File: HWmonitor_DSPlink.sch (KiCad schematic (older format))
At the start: 99 parts, among them J1 Mini USB - Type B, J2 IDC-Header 2x4, T1 760390014, U1 FT232RL, U10 OPA197xDBV, U11 OPA197xDBV, U12 USBLC6-2SC6, U2 ISO7830DWW, U3 ISO7821DWW, U4 SN6501DBVR, U5 TL431BCDBZ, U6 AD5324ARMZ, U7 TLV70450DBVT, U8 OPA197xDBV, U9 OPA197xDBV, X1 Conn_Coaxial, X2 Conn_Coaxial, X3 Conn_Coaxial, X4 Conn_Coaxial

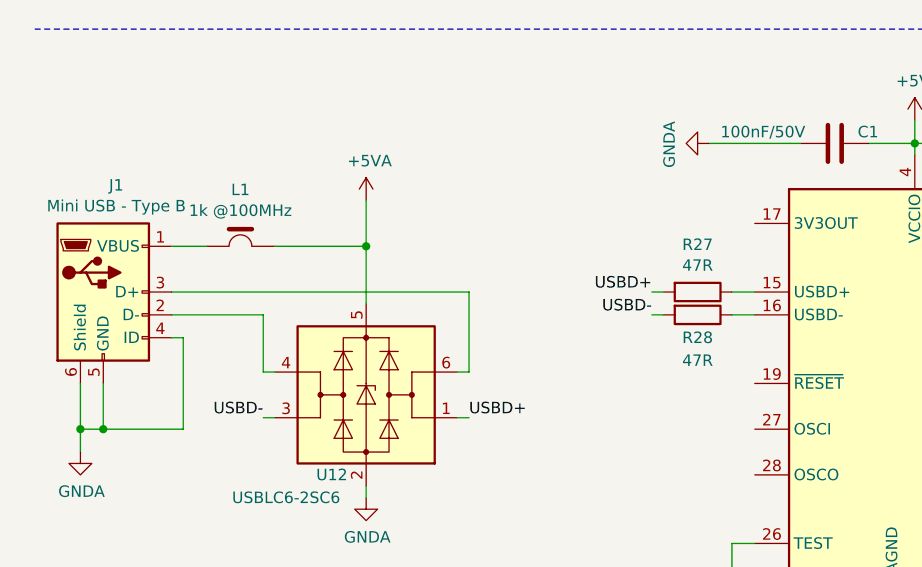
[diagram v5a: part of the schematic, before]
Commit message: modified layout ftdi chip, added 3.3V capacitor
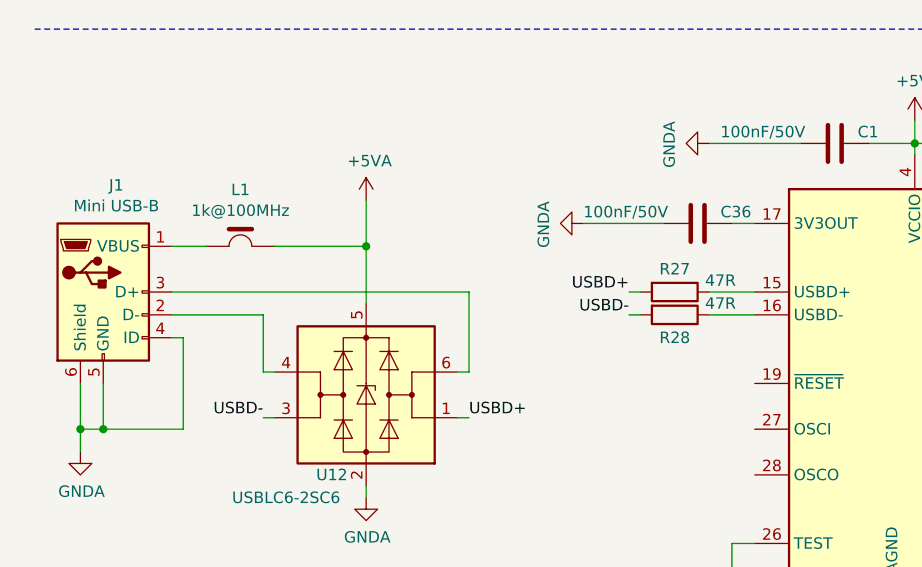
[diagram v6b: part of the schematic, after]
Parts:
- added C36: 100nF/50V, Capacitor_SMD:C_0603_1608Metric, symbol Device:C
- J1: value Mini USB - Type B -> Mini USB-B
- L1: value 1k @100MHz -> 1k@100MHz
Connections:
- net GNDA: now also C36.1
- net at U1.17 (3V3OUT): now also C36.2
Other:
- moved on the sheet: R27, R28
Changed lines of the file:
@@
 AR Path="/60E0A151/610C42BB" Ref="J?"  Part="1"
 F 0 "J1" H 1307 9517 50  0000 C CNN
-F 1 "Mini USB - Type B" H 1307 9426 50  0000 C CNN
+F 1 "Mini USB-B" H 1307 9426 50  0000 C CNN
 F 2 "Connector_USB:USB_Mini-B_Lumberg_2486_01_Horizontal" H 1400 9000 50  0001 C CNN
 F 3 "~" H 1400 9000 50  0001 C CNN
@@
 P 1850 8850
 F 0 "L1" H 1850 9097 50  0000 C CNN
-F 1 "1k @100MHz" H 1850 9006 50  0000 C CNN
+F 1 "1k@100MHz" H 1850 9006 50  0000 C CNN
 F 2 "Inductor_SMD:L_0603_1608Metric" H 1850 8850 50  0001 C CNN
 F 3 "" H 1850 8850 50  0001 C CNN
@@
 $EndComp
 $Comp
-L Device:R R27
-U 1 1 5FEE3BD6
-P 3850 9050
-F 0 "R27" V 3643 9050 50  0000 C CNN
-F 1 "47R" V 3734 9050 50  0000 C CNN
-F 2 "Resistor_SMD:R_0603_1608Metric" V 3780 9050 50  0001 C CNN
-F 3 "~" H 3850 9050 50  0001 C CNN
-	1    3850 9050
-	0    1    1    0
-$EndComp
-$Comp
 L Device:R R28
 U 1 1 5FEE4D7D
-P 3850 9150
-F 0 "R28" V 3950 9150 50  0000 C CNN
-F 1 "47R" V 4050 9150 50  0000 C CNN
-F 2 "Resistor_SMD:R_0603_1608Metric" V 3780 9150 50  0001 C CNN
-F 3 "~" H 3850 9150 50  0001 C CNN
-	1    3850 9150
-	0    1    1    0
-$EndComp
-Wire Wire Line
-	4000 9050 4100 9050
-Wire Wire Line
-	4000 9150 4100 9150
+P 3750 9150
+F 0 "R28" V 3850 9150 50  0000 C CNN
+F 1 "47R" V 3700 9350 50  0000 C CNN
+F 2 "Resistor_SMD:R_0603_1608Metric" V 3680 9150 50  0001 C CNN
+F 3 "~" H 3750 9150 50  0001 C CNN
+	1    3750 9150
+	0    1    1    0
+$EndComp
+Wire Wire Line
+	3900 9050 4100 9050
+Wire Wire Line
+	3900 9150 4100 9150
 $Comp
 L Power_Protection:USBLC6-2SC6 U12
@@
 	4300 8400 3900 8400
 Wire Wire Line
-	3700 9050 3650 9050
-Wire Wire Line
-	3700 9150 3650 9150
-Text Label 3650 9050 2    50   ~ 0
+	3600 9050 3550 9050
+Wire Wire Line
+	3600 9150 3550 9150
+Text Label 3550 9050 2    50   ~ 0
 USBD+
-Text Label 3650 9150 2    50   ~ 0
+Text Label 3550 9150 2    50   ~ 0
 USBD-
 Wire Wire Line
@@
 	1    0    0    -1
 $EndComp
+$Comp
+L Device:C C36
+U 1 1 5FE68C23
+P 3850 8750
+F 0 "C36" V 3800 8650 50  0000 R CNN
+F 1 "100nF/50V" V 3800 9250 50  0000 R CNN
+F 2 "Capacitor_SMD:C_0603_1608Metric" H 3888 8600 50  0001 C CNN
+F 3 "~" H 3850 8750 50  0001 C CNN
+	1    3850 8750
+	0    -1   1    0
+$EndComp
+$Comp
+L Device:R R27
+U 1 1 5FEE3BD6
+P 3750 9050
+F 0 "R27" V 3650 9050 50  0000 C CNN
+F 1 "47R" V 3700 9250 50  0000 C CNN
+F 2 "Resistor_SMD:R_0603_1608Metric" V 3680 9050 50  0001 C CNN
+F 3 "~" H 3750 9050 50  0001 C CNN
+	1    3750 9050
+	0    1    1    0
+$EndComp
+Wire Wire Line
+	4000 8750 4100 8750
+$Comp
+L power:GNDA #PWR0101
+U 1 1 5FEF754F
+P 3350 8750
+AR Path="/5FEF754F" Ref="#PWR0101"  Part="1"
+AR Path="/60E0A151/5FEF754F" Ref="#PWR?"  Part="1"
+F 0 "#PWR0101" H 3350 8500 50  0001 C CNN
+F 1 "GNDA" H 3355 8577 50  0000 C CNN
+F 2 "" H 3350 8750 50  0001 C CNN
+F 3 "" H 3350 8750 50  0001 C CNN
+	1    3350 8750
+	0    1    1    0
+$EndComp
+Wire Wire Line
+	3700 8750 3350 8750
 $EndSCHEMATC

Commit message: last modifications, documents generated
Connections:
- net GNDA: no longer J1.4 (ID)
- no-connect marks 0 -> 15
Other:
- note added: "HWmonitor & DSPcom debug tool"
- note removed: "HWmonitor & DSPlink debug tool"
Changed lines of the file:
@@
-$EndComp
-$Comp
-L Connector:USB_B_Mini J1
-U 1 1 610C42BB
-P 1250 9050
-AR Path="/610C42BB" Ref="J1"  Part="1"
-AR Path="/60E0A151/610C42BB" Ref="J?"  Part="1"
-F 0 "J1" H 1307 9517 50  0000 C CNN
-F 1 "Mini USB-B" H 1307 9426 50  0000 C CNN
-F 2 "Connector_USB:USB_Mini-B_Lumberg_2486_01_Horizontal" H 1400 9000 50  0001 C CNN
-F 3 "~" H 1400 9000 50  0001 C CNN
-F 4 "65100516121" H 1250 9050 50  0001 C CNN "MPN"
-	1    1250 9050
-	1    0    0    -1
 $EndComp
 $Comp
@@
 Connection ~ 4700 10500
 Wire Wire Line
-	1550 9250 1600 9250
-Wire Wire Line
-	1600 9250 1600 9650
-Wire Wire Line
-	1600 9650 1250 9650
-Wire Wire Line
 	1250 9650 1250 9450
 Wire Wire Line
@@
 Wire Wire Line
 	1150 9650 1250 9650
-Connection ~ 1250 9650
 $Comp
 L #MyLibrary:Ferrite_Bead L1
@@
 $EndComp
 Text Notes 12350 10350 0    126  Italic 25
-HWmonitor & DSPlink debug tool
+HWmonitor & DSPcom debug tool
 $Comp
 L #MyLibrary:TLV70450DBVT U7
@@
 Wire Wire Line
 	3700 8750 3350 8750
+NoConn ~ 4100 9450
+NoConn ~ 4100 9650
+NoConn ~ 4100 9850
+NoConn ~ 5700 10150
+NoConn ~ 5700 10050
+NoConn ~ 5700 9950
+NoConn ~ 5700 9450
+NoConn ~ 5700 9350
+NoConn ~ 5700 9250
+NoConn ~ 5700 9150
+NoConn ~ 5700 9050
+NoConn ~ 5700 8950
+NoConn ~ 2750 5400
+NoConn ~ 8900 3600
+$Comp
+L Connector:USB_B_Mini J1
+U 1 1 610C42BB
+P 1250 9050
+AR Path="/610C42BB" Ref="J1"  Part="1"
+AR Path="/60E0A151/610C42BB" Ref="J?"  Part="1"
+F 0 "J1" H 1307 9517 50  0000 C CNN
+F 1 "Mini USB-B" H 1307 9426 50  0000 C CNN
+F 2 "Connector_USB:USB_Mini-B_Lumberg_2486_01_Horizontal" H 1400 9000 50  0001 C CNN
+F 3 "~" H 1400 9000 50  0001 C CNN
+F 4 "65100516121" H 1250 9050 50  0001 C CNN "MPN"
+	1    1250 9050
+	1    0    0    -1
+$EndComp
+NoConn ~ 1550 9250
 $EndSCHEMATC

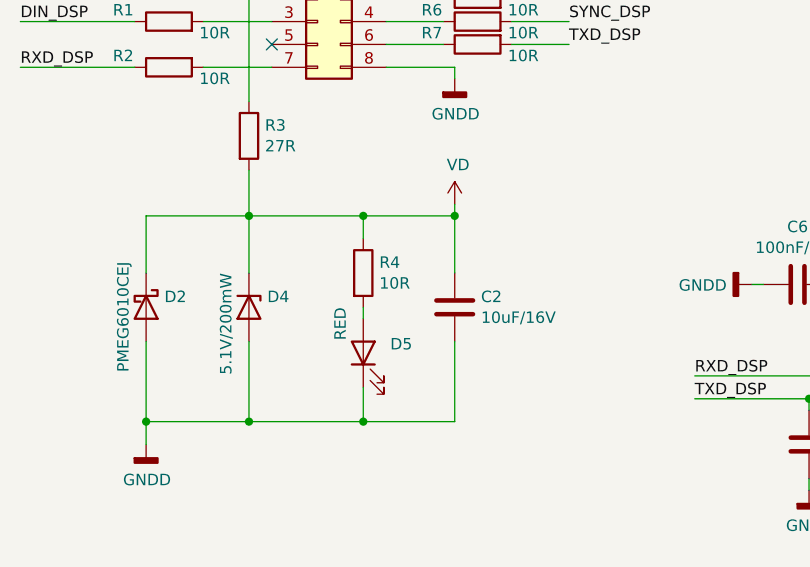
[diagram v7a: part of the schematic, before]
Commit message: BOM bug, LED resistor to 270R
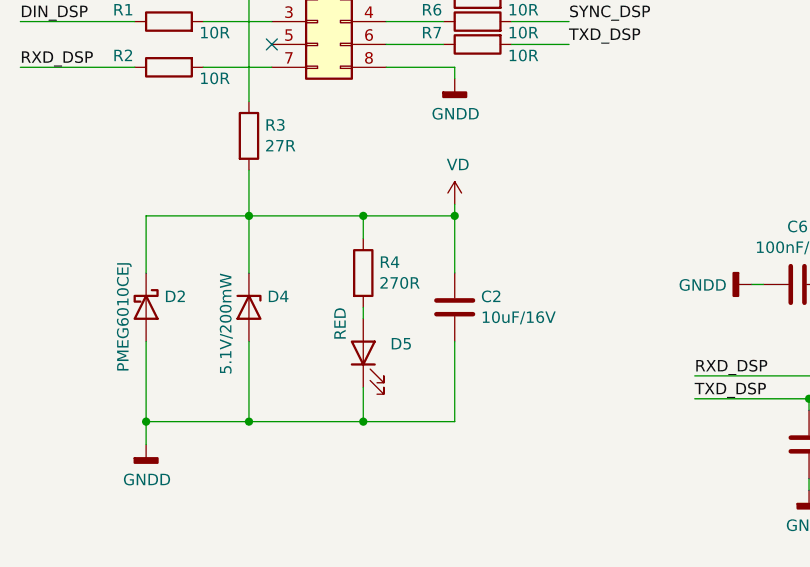
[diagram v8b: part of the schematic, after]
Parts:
- R4: value 10R -> 270R
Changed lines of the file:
@@
 P 3150 6400
 F 0 "R4" H 3220 6446 50  0000 L CNN
-F 1 "10R" H 3220 6355 50  0000 L CNN
+F 1 "270R" H 3220 6355 50  0000 L CNN
 F 2 "Resistor_SMD:R_0603_1608Metric" V 3080 6400 50  0001 C CNN
 F 3 "~" H 3150 6400 50  0001 C CNN
